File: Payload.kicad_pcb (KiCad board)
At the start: 2 copper layers, 119 parts, among them J1 conn_USB-A-(UE27AC54100), SW1 SW_Push, SW2 SW_Push, U1 STM32-(STM32H745ZIT6), U10 LDO_5-1.8V-(MIC5504-1.8YM5-TR), U11 ICU-Gyro-(ICM-20948), U12 AS5F32G04SNDA-08LIN(mémoire), U13 AS5F32G04SNDA-08LIN(mémoire), U14 conn-fem-90deg-(PPPC062LJBN-R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, U2 INA2331AIPWR, U3 LMC6482IN, U4 LMC6482IN, U5 LMC6482IN, U6 INA2331AIPWR, U7 LMC6482IN, U8 LM2576HVS-5, U9 LDO 5-3.3V-(MIC5504-3.3YM5-TR)

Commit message: PCB1
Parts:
- moved C31 123.0 mm to (169.9, 63.8), turned to 180 degrees
- moved C23 122.3 mm to (194.2, 72.5), turned to 90 degrees
- moved R8 119.1 mm to (202.3, 70.8)
- moved C16 115.2 mm to (192.2, 72.6), turned to 90 degrees
- moved D4 111.6 mm to (20.0, 17.3)
- moved C35 109.4 mm to (158.0, 72.8), turned to 90 degrees
- moved FB1 105.3 mm to (24.7, 17.3)
- moved R9 101.4 mm to (173.4, 64.2), turned to 90 degrees
- moved C15 100.1 mm to (185.1, 94.6)
- moved F2 99.4 mm to (21.0, 20.4), turned to 90 degrees
- moved C14 98.8 mm to (187.8, 92.3), turned to 90 degrees
- moved R12 98.3 mm to (194.6, 88.1), turned to 180 degrees
- moved C8 97.2 mm to (185.1, 92.6)
- moved R31 96.6 mm to (50.7, 17.3)
- moved R32 96.6 mm to (50.7, 19.8)
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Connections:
- RV1 pad 3: GND -> Net-(U2-RGA)
- RV5 pad 3: GND -> Net-(U6-RGA)
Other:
- board text added: "Strain Gauge"
- board text added: "Thermistance"
- board text added: "Vibro1"
- board text added: "Vusb"

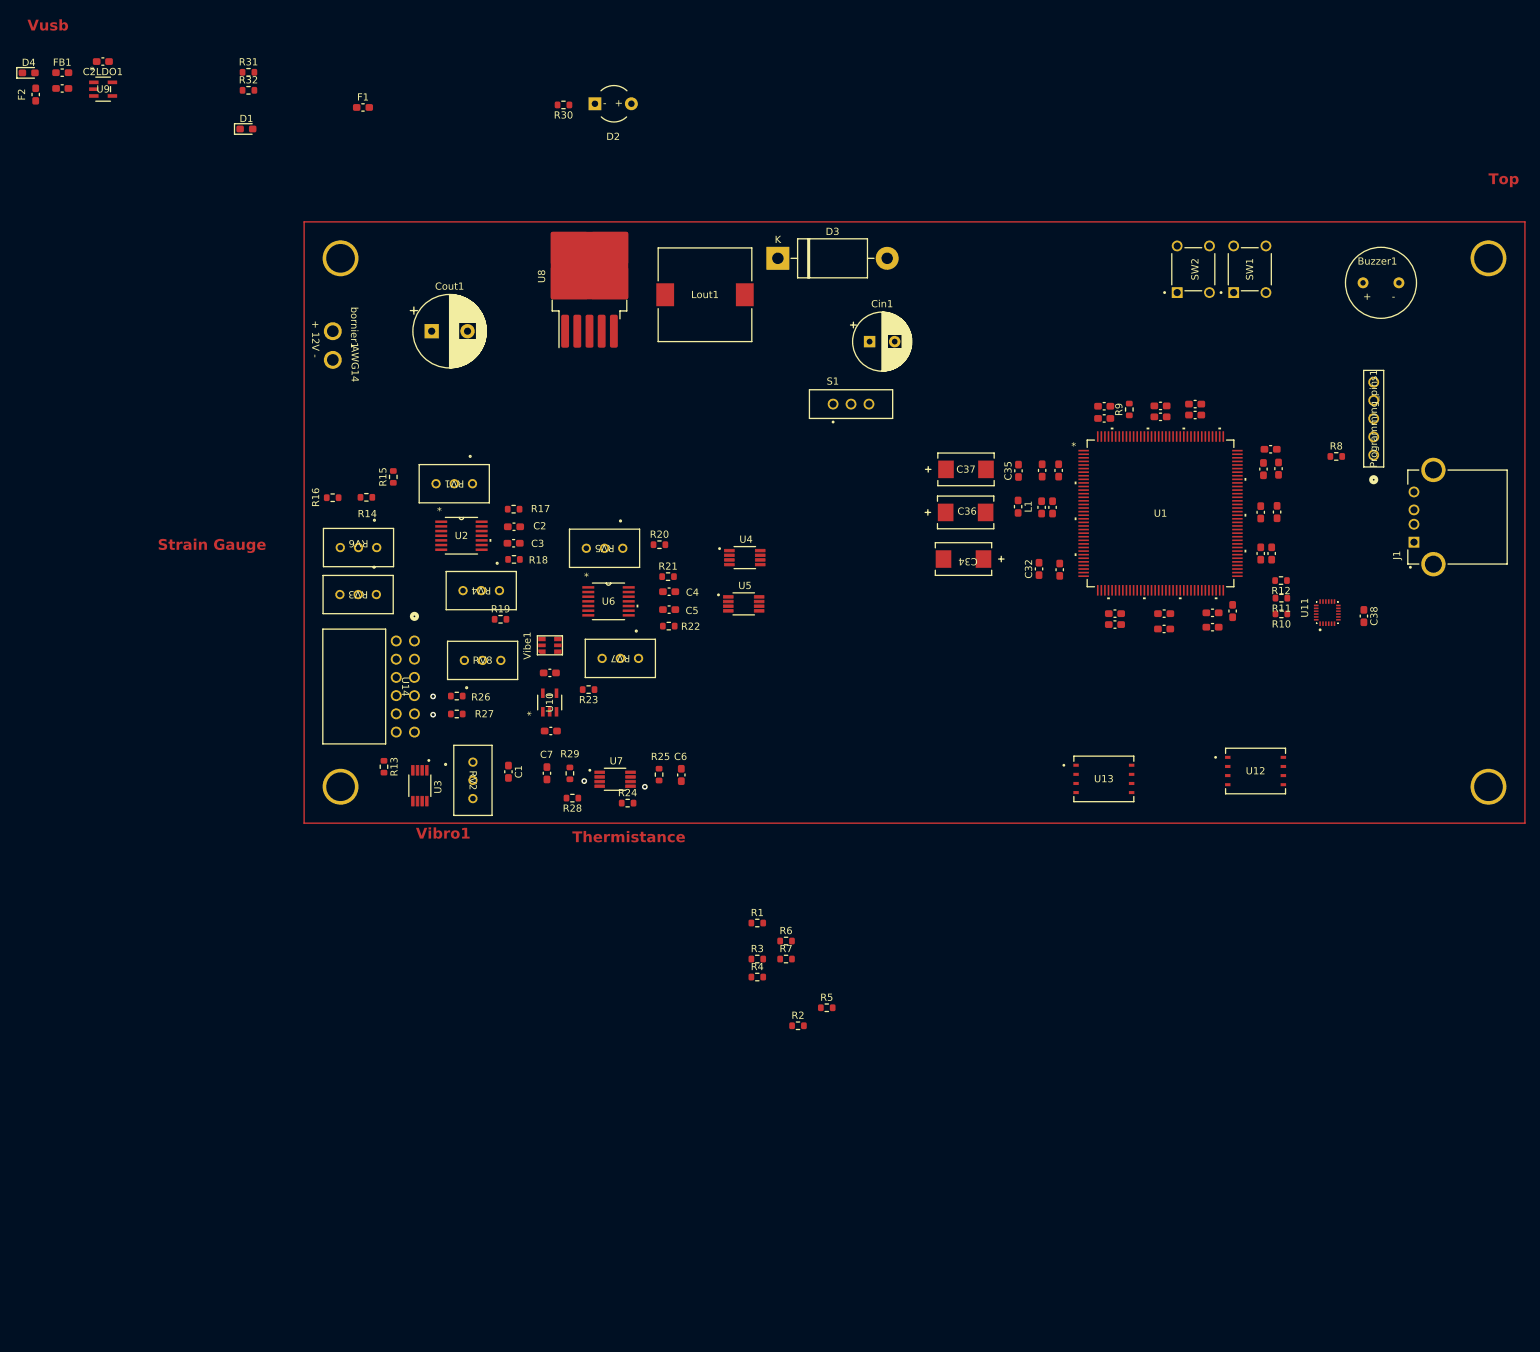
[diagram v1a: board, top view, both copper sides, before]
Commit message: Remplacement du Buck par un LDO
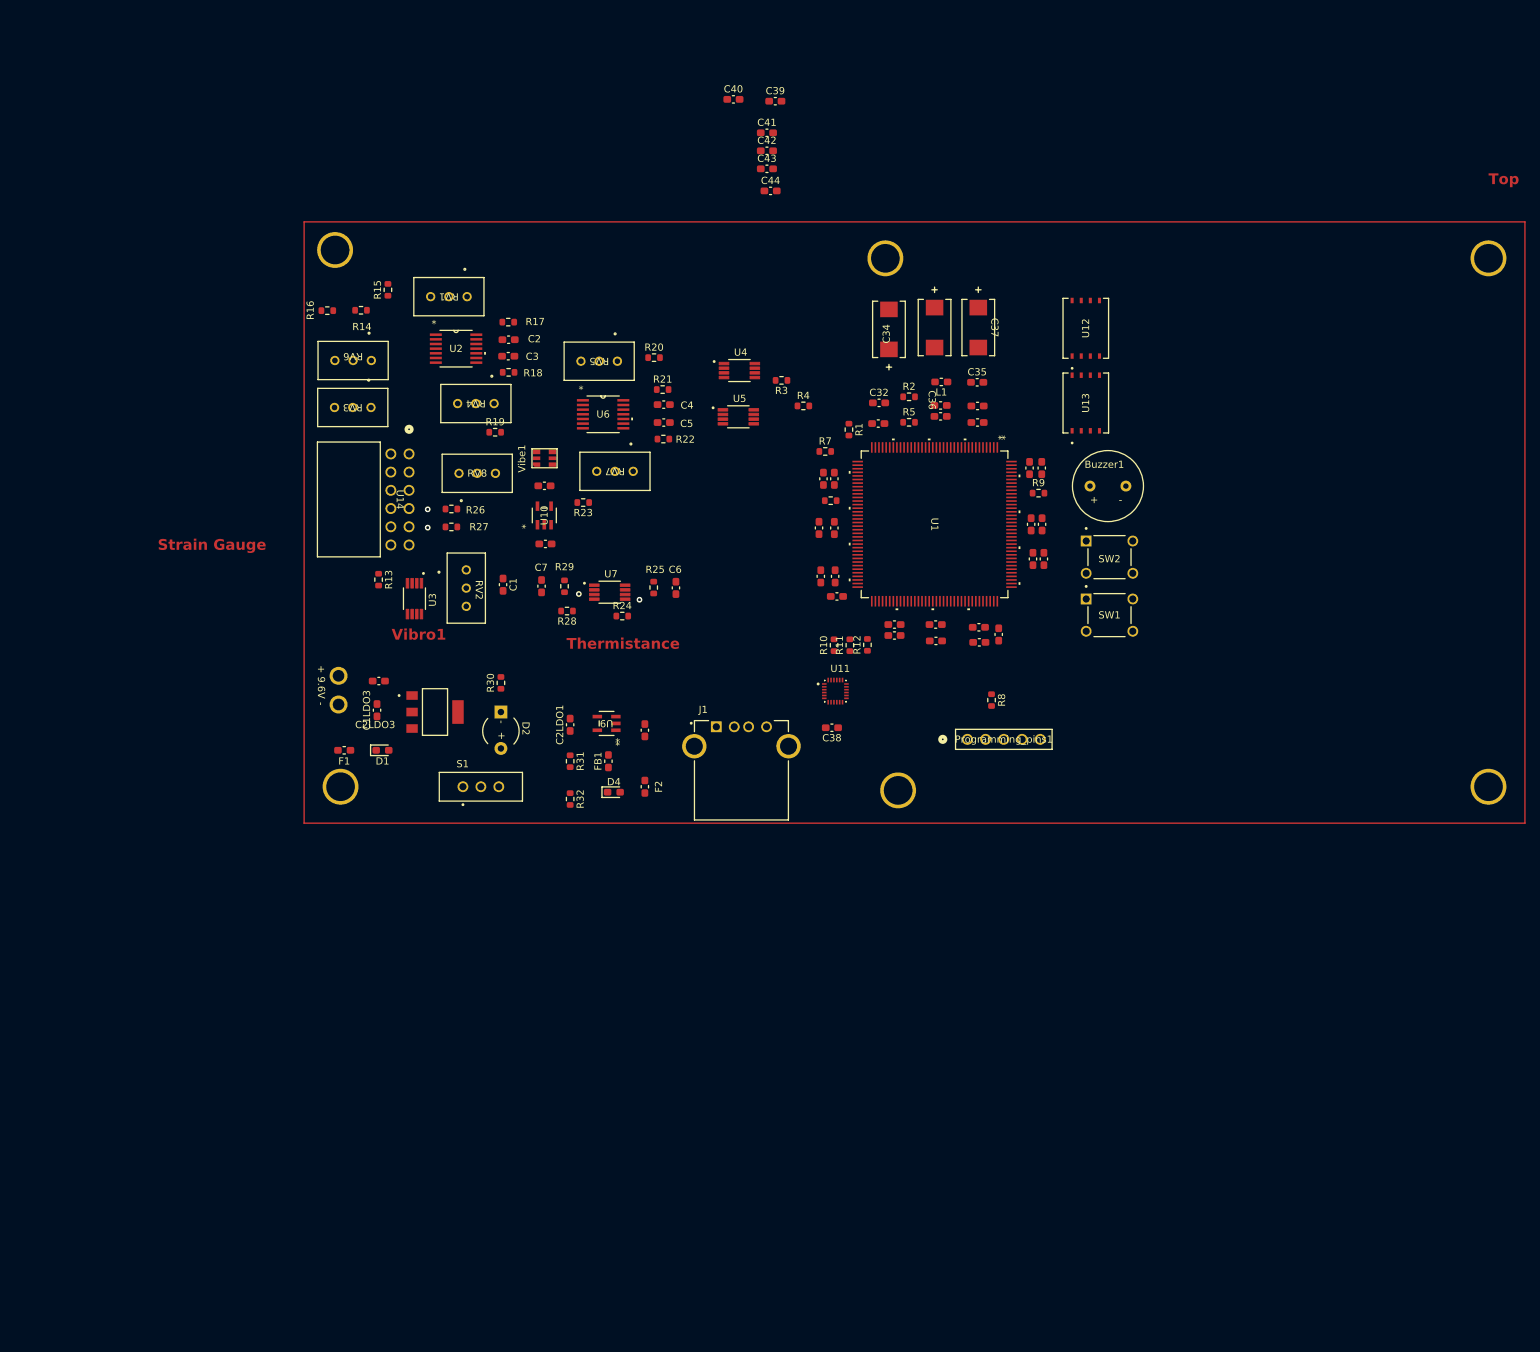
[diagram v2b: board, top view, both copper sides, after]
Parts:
- removed Cin1: 100u, Capacitor_THT:CP_Radial_D8.0mm_P3.50mm
- removed Cout1: 1000u, Capacitor_THT:CP_Radial_D10.0mm_P5.00mm
- removed D3: 1N5820, Diode_THT:D_DO-201AD_P15.24mm_Horizontal
- removed Lout1: 100u, GAUL-Empreintes:induct-100uH-(IND_YUDEN_NS12575_YDN)
- removed U8: LM2576HVS-5, Package_TO_SOT_SMD:TO-263-5_TabPin3
- added ?: , , F.Cu at (141.2, 117.3)
- added ?: , , F.Cu at (139.4, 43.2)
- added C1LDO3: 10uF, Capacitor_SMD:C_0603_1608Metric_Pad1.08x0.95mm_HandSolder, F.Cu at (68.6, 106.2)
- added C2LDO3: 10uF, Capacitor_SMD:C_0603_1608Metric_Pad1.08x0.95mm_HandSolder, F.Cu at (68.8, 102.1)
- added C39: 10nF, Capacitor_SMD:C_0603_1608Metric_Pad1.08x0.95mm_HandSolder, F.Cu at (124.1, 21.3)
- added C40: 10nF, Capacitor_SMD:C_0603_1608Metric_Pad1.08x0.95mm_HandSolder, F.Cu at (118.3, 21.0)
- added C41: 10nF, Capacitor_SMD:C_0603_1608Metric_Pad1.08x0.95mm_HandSolder, F.Cu at (122.9, 25.7)
- added C42: 10nF, Capacitor_SMD:C_0603_1608Metric_Pad1.08x0.95mm_HandSolder, F.Cu at (122.9, 28.2)
- added C43: 10nF, Capacitor_SMD:C_0603_1608Metric_Pad1.08x0.95mm_HandSolder, F.Cu at (122.9, 30.7)
- added C44: 10nF, Capacitor_SMD:C_0603_1608Metric_Pad1.08x0.95mm_HandSolder, F.Cu at (123.4, 33.8)
- added VR1: LDO12-3V3-(TS1117BCW33_RPG), GAUL-Empreintes:LDO12-3V3-(TS1117BCW33_RPG), F.Cu at (76.7, 106.4)
- moved D4 129.3 mm to (101.6, 117.6)
- moved F2 128.5 mm to (105.9, 116.8), turned to -90 degrees
- moved FB1 122.5 mm to (100.8, 113.3), turned to 90 degrees
- moved C1LDO1 120.8 mm to (105.9, 109.0), turned to 90 degrees
- moved C2LDO1 113.1 mm to (95.5, 108.2), turned to 90 degrees
- moved U9 112.9 mm to (100.6, 108.0), turned to 180 degrees
- moved R32 108.5 mm to (95.5, 118.6), turned to -90 degrees
- moved R31 106.0 mm to (95.5, 113.3), turned to -90 degrees
- moved J1 98.2 mm to (119.4, 108.5), turned to 0 degrees
- moved F1 89.6 mm to (64.0, 111.8)
- moved R2 89.0 mm to (142.7, 62.5)
- moved D1 88.7 mm to (69.3, 111.8)
- moved D2 84.8 mm to (80.8, 109.0), turned to -90 degrees
- moved R5 82.4 mm to (142.7, 66.0)
- moved R30 81.0 mm to (85.9, 102.4), turned to 90 degrees
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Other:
- board text removed: "Vusb"

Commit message: Routing commencé
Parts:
- removed R10, R11, R12: 0, Resistor_SMD:R_0603_1608Metric
- added ?: , , F.Cu at (63.2, 65.8)
- added ?: , , F.Cu at (63.2, 91.7)
- moved C39 91.7 mm to (72.0, 96.8), turned to 90 degrees
- moved C42 67.4 mm to (103.9, 92.8), turned to 180 degrees
- moved H4 53.3 mm to (170.2, 122.0)
- moved H3 53.1 mm to (170.4, 48.3)
- moved C40 49.1 mm to (116.1, 70.1), turned to 180 degrees
- moved ? 45.8 mm to (99.3, 65.3)
- moved C44 44.8 mm to (83.6, 54.1)
- moved C43 33.3 mm to (104.4, 58.4)
- moved R2 30.8 mm to (114.8, 75.4), turned to 180 degrees
- moved C41 27.8 mm to (116.1, 52.6)
- moved SW1 21.1 mm to (160.3, 111.3)
- moved C34 16.6 mm to (124.0, 48.5)
- moved SW2 15.3 mm to (160.3, 96.0)
- moved R20 14.0 mm to (94.5, 51.1), turned to 90 degrees
- moved RV5 14.0 mm to (101.9, 43.5)
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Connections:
- U1 pad 72: Net-(U1A-PB12) -> NSS
- U1 pad 73: Net-(U1A-PB13) -> SCK
- U1 pad 75: Net-(U1A-PB15) -> MOSI
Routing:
- net GND: track 0.00 -> 46.6 mm, vias 0 -> 12
- net /circuits_capteurs/Suiveur: track 0.00 -> 40.9 mm, vias 0 -> 2
- net /circuits_capteurs/IN-: track 0.00 -> 30.5 mm, vias 0 -> 2
- net Net-(U2-VOUTB): track 0.00 -> 15.8 mm
- net Net-(U6-RGA): track 0.00 -> 14.2 mm
- net Net-(U2-VOUTA): track 0.00 -> 13.8 mm
- net SG3_4: track 0.00 -> 9.84 mm
- net Net-(U2-RGB): track 0.00 -> 9.72 mm
- net Net-(U2-RGA): track 0.00 -> 6.48 mm
- net /circuits_capteurs/Suiveur1: track 0.00 -> 4.11 mm
- net Net-(U6-VOUTA): track 0.00 -> 2.54 mm
- net +3.3V: track 0.00 -> 1.74 mm, vias 0 -> 1
- net (no net): vias 4 -> 2
- added copper zone on In1.Cu, net +3.3V
- added copper zone on In2.Cu, net GND
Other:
- board outline added: 117.1 x 83.8 mm
- copper layers 2 -> 4
- board text removed: "Strain Gauge"
- board text removed: "Thermistance"
- board text removed: "Top"
- board text removed: "Vibro1"

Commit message: PayPay
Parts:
- moved R5 9.81 mm to (126.8, 62.0), turned to 180 degrees
- moved F2 8.06 mm to (107.8, 109.0)
- moved D4 4.67 mm to (104.8, 114.2)
- moved C32 4.07 mm to (132.2, 64.0), turned to 180 degrees
- moved F1 3.59 mm to (67.6, 111.8)
- moved D1 3.26 mm to (72.6, 111.8), turned to 180 degrees
- moved C39 3.16 mm to (73.4, 99.6), turned to -90 degrees
- moved C24 2.91 mm to (141.8, 64.0)
- moved U3 1.79 mm to (75.1, 93.4)
- moved R13 1.77 mm to (70.8, 92.6)
- moved C30 1.64 mm to (146.2, 63.9)
- moved C31 1.51 mm to (157.0, 72.6)
- moved C33 1.43 mm to (132.2, 66.4), turned to 180 degrees
- moved R9 1.28 mm to (155.2, 76.4)
- moved C19 1.22 mm to (157.0, 79.8)
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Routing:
- net GND: track 46.6 -> 183.3 mm, vias 12 -> 27
- net +3.3V: track 1.74 -> 104.6 mm, vias 1 -> 15
- net Net-(VR1-OUTPUT): track 0.00 -> 24.0 mm
- net Net-(U9-VOUT): track 0.00 -> 13.2 mm
- net Net-(U9-VIN): track 0.00 -> 12.9 mm
- net Net-(D1-K): track 0.00 -> 8.62 mm
- net Net-(F1-Pad1): track 0.00 -> 7.87 mm
- net Vusb: track 0.00 -> 6.36 mm
- net /circuit_alimentation/Vcap1(68): track 0.00 -> 6.31 mm
- net Net-(U3-NEGA): track 0.00 -> 5.98 mm
- net /circuit_alimentation/Vcap2(103): track 0.00 -> 5.82 mm
- net Net-(D4-A): track 0.00 -> 5.21 mm
- net Net-(U1B-BOOT0): track 0.00 -> 3.50 mm
- net Net-(D1-A): track 0.00 -> 3.27 mm
- net Net-(D2--): track 0.00 -> 3.24 mm
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
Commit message: Routing terminé
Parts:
- removed ? (x4): , 
- added H5: ~, GAUL-Empreintes:Ground_mounting_hole_1mm, F.Cu at (63.2, 70.9)
- added H6: ~, GAUL-Empreintes:Ground_mounting_hole_1mm, F.Cu at (99.3, 70.4)
- added H7: ~, GAUL-Empreintes:Ground_mounting_hole_1mm, F.Cu at (135.9, 122.4)
- added H8: ~, GAUL-Empreintes:Ground_mounting_hole_1mm, F.Cu at (63.3, 96.8)
- moved U12 54.8 mm to (118.2, 85.3)
- moved R7 9.58 mm to (119.4, 77.9)
- moved R5 3.05 mm to (127.0, 65.0)
- moved R1 2.86 mm to (127.0, 68.9)
- moved R6 0.99 mm to (125.0, 76.5)
- moved C44 0.86 mm to (84.4, 54.1)
- moved C12 0.54 mm to (123.6, 73.6)
- moved C26 0.54 mm to (126.2, 73.6)
- moved R22 0.51 mm to (106.2, 66.3)
- moved R2 0.21 mm to (114.9, 75.6)
- moved U10 0.15 mm to (102.7, 81.1)
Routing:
- net GND: track 183.3 -> 284.9 mm, vias 27 -> 44
- net +3.3V: track 104.6 -> 205.1 mm, vias 15 -> 28
- net USB_check: track 2.87 -> 64.8 mm, vias 0 -> 2
- net QUADSPI_CLK: track 0.00 -> 53.4 mm, vias 0 -> 2
- net /circuit_alimentation/VFBSMPS: track 0.00 -> 52.9 mm, vias 0 -> 3
- net ADC123_INP10-Vibro2: track 0.00 -> 50.7 mm
- net +1V8: track 0.00 -> 47.0 mm, vias 0 -> 2
- net ADC1_INP16-Therm2: track 0.00 -> 41.2 mm, vias 0 -> 2
- net QUADSPI_BK2_NCS: track 0.00 -> 38.1 mm, vias 0 -> 2
- net USB_D-: track 0.00 -> 37.9 mm, vias 0 -> 2
- net USB_D+: track 0.00 -> 37.3 mm, vias 0 -> 2
- net QUADSPI_BK1_NCS: track 0.00 -> 35.4 mm
- net ADC12_INP3-Therm1: track 0.00 -> 34.9 mm
- net SWO: track 0.00 -> 34.6 mm, vias 0 -> 1
- net Net-(U6-RGB): track 0.00 -> 34.5 mm, vias 0 -> 1
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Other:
- board text added: "3V3"
- board text added: "CLK"
- board text added: "GND"
- board text added: "IO"
- board text added: "SWO"
